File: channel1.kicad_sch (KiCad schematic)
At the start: 58 parts, among them IC1 TLV73325PDBVT, IC2 TLV73312PDBVT, J2 HDMI-A_Molex_471511001, J3 5051101992, U1 TC358742XBG, U2 TPD8S009DSMR, U3 PCA9517ATP, Y1 Oscillator_27MHz_TXC_7C

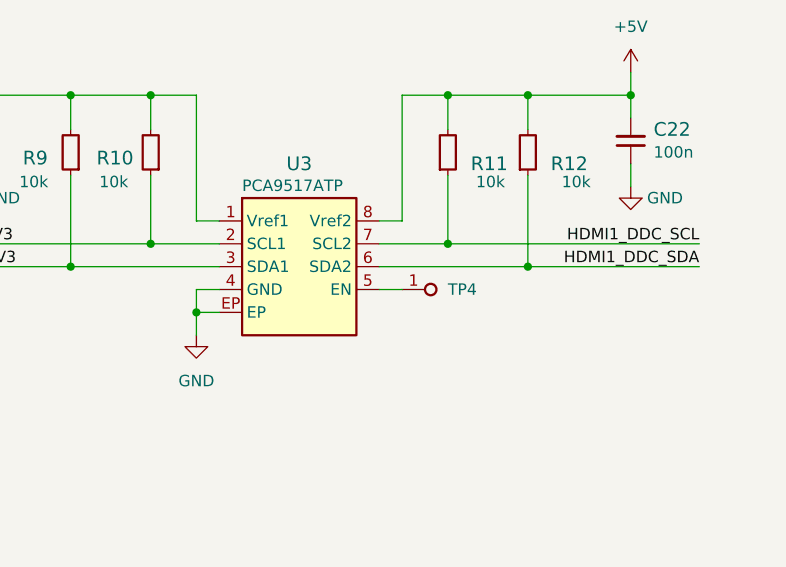
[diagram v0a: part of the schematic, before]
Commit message: [#58304] Update PCA9517ATP symbol
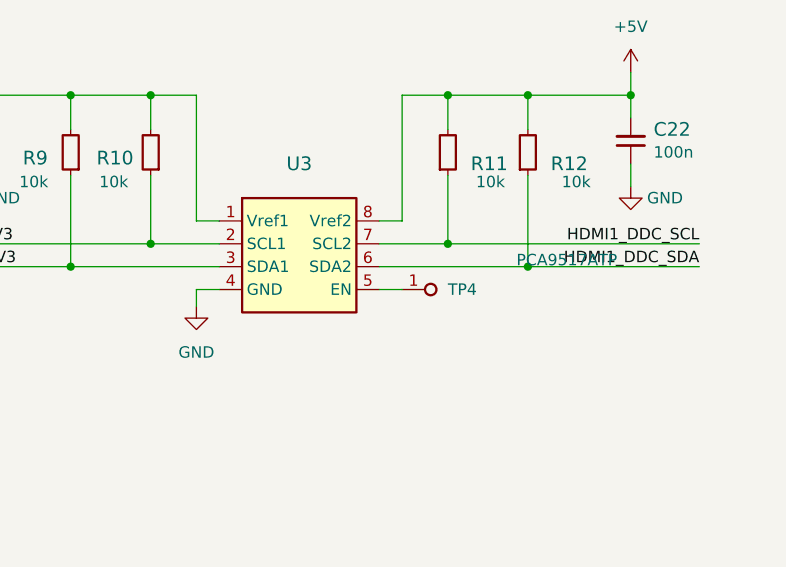
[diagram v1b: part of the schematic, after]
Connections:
- net GND: now also U3.9 (GND); no longer U3.EP
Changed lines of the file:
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@@
   (junction (at 330.2 205.74) (diameter 0) (color 0 0 0 0)
   )
-  (junction (at 332.74 107.95) (diameter 0) (color 0 0 0 0)
-  )
   (junction (at 358.14 171.45) (diameter 0) (color 0 0 0 0)
   )
@@
     (stroke (width 0) (type default))
   )
-  (wire (pts (xy 332.74 107.95) (xy 332.74 110.49))
+  (wire (pts (xy 332.74 105.41) (xy 332.74 107.315))
     (stroke (width 0) (type default))
   )
@@
     (stroke (width 0) (type default))
   )
-  (wire (pts (xy 332.74 107.95) (xy 332.74 105.41))
-    (stroke (width 0) (type default))
-  )
   (wire (pts (xy 195.58 215.9) (xy 198.12 215.9))
     (stroke (width 0) (type default))
@@
     (stroke (width 0) (type default))
   )
-  (wire (pts (xy 332.74 107.95) (xy 335.28 107.95))
-    (stroke (width 0) (type default))
-  )
   (wire (pts (xy 93.98 259.08) (xy 93.98 261.62))
     (stroke (width 0) (type default))
@@
       (effects (font (size 1.524 1.524)))
     )
-    (property "Value" "PCA9517ATP" (at 339.09 94.615 0)
-      (effects (font (size 1.27 1.27) (thickness 0.15)) (justify left bottom) hide)
+    (property "Value" "PCA9517ATP" (at 368.3 102.87 0)
+      (effects (font (size 1.27 1.27) (thickness 0.15)) (justify left bottom))
     )
     (property "Footprint" "antmicro-footprints:SOT1069-2" (at 368.3 105.41 0)
@@
       (effects (font (size 1.27 1.27) (thickness 0.15)) (justify left bottom) hide)
     )
-    (property "MPN" "PCA9517ATP" (at 337.82 94.615 0)
-      (effects (font (size 1.27 1.27) (thickness 0.15)) (justify left bottom))
+    (property "MPN" "PCA9517ATP" (at 368.3 110.49 0)
+      (effects (font (size 1.27 1.27) (thickness 0.15)) (justify left bottom) hide)
     )
     (property "Manufacturer" "NXP" (at 368.3 113.03 0)
@@
     (pin "7")
     (pin "8")
-    (pin "EP")
+    (pin "9")
     (instances
       (project "antmicro-hdmi-mipi-bridge-hw"
@@
     )
   )
-  (symbol (lib_id "antmicropower:GND") (at 332.74 110.49 0) (mirror y) (unit 1)
+  (symbol (lib_id "antmicropower:GND") (at 332.74 107.315 0) (mirror y) (unit 1)
     (in_bom yes) (on_board yes) (dnp no) (fields_autoplaced)
-    (property "Reference" "#PWR0115" (at 332.74 116.84 0)
+    (property "Reference" "#PWR0115" (at 332.74 113.665 0)
       (effects (font (size 1.27 1.27)) hide)
     )
-    (property "Value" "GND" (at 332.74 115.57 0)
+    (property "Value" "GND" (at 332.74 112.395 0)
       (effects (font (size 1.27 1.27)))
     )
-    (property "Footprint" "" (at 332.74 110.49 0)
+    (property "Footprint" "" (at 332.74 107.315 0)
       (effects (font (size 1.27 1.27)) hide)
     )
-    (property "Datasheet" "" (at 332.74 110.49 0)
+    (property "Datasheet" "" (at 332.74 107.315 0)
       (effects (font (size 1.27 1.27)) hide)
     )

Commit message: [#58304] kmake dnp
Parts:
- J3: DNP (none) -> DNP
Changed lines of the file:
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@@
     (pin "8")
     (pin "9")
-    (pin "8")
     (instances
       (project "antmicro-hdmi-mipi-bridge-hw"
@@
       (effects (font (size 1.27 1.27) (thickness 0.15)) (justify left bottom) hide)
     )
-    (pin "1")
+    (property "DNP" "DNP" (at 0.0 0.0 0)
+      (effects (font (size 1.0 1.0)))
+    )
+    (pin "1")
